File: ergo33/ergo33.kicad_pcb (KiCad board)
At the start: 2 copper layers, 171.4 x 117.8 mm, 113 parts, among them SW1 SW_Push, SW46 Rotary_Encoder_Switch, U1 ATmega32U4-AU, Y1 16MHz

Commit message: Start trace layout
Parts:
- removed F2: 500mA, Fuse:Fuse_1206_3216Metric
- added JP4: SolderJumper_2_Open, Jumper:SolderJumper-2_P1.3mm_Open_Pad1.0x1.5mm, B.Cu at (176.3, 40.5)
- SW46: footprint tunks-parts:RotaryEncoder_Alps_EC11E-Switch_Vertical_H20mm_30mm_knob -> Rotary_Encoder:RotaryEncoder_Alps_EC11E-Switch_Vertical_H20mm
- moved JP1 70.8 mm to (227.0, 24.2)
- moved R4 55.1 mm to (169.7, 76.0), turned to 0 degrees
- moved LED10 54.1 mm to (210.6, 106.7)
- moved C18 52.7 mm to (204.8, 106.5)
- moved C1 47.5 mm to (186.5, 70.5)
- moved LED7 46.9 mm to (78.9, 128.7)
- moved C15 46.9 mm to (74.1, 129.4)
- moved C5 45.6 mm to (179.7, 76.0)
- moved C2 42.0 mm to (186.5, 61.4)
- moved Y1 39.5 mm to (186.8, 65.8), turned to 135 degrees
- moved C17 38.8 mm to (152.6, 146.6)
- moved LED9 38.8 mm to (157.3, 145.8)
- moved SW1 38.2 mm to (186.4, 47.5), turned to 90 degrees
- moved U1 38.0 mm to (174.9, 66.2), turned to 270 degrees
- moved JLED1 37.7 mm to (210.3, 89.8)
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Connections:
- net Net-(F1-Pad1) renamed PWR_IN
- JP1 pad 1: LEDS -> (no net)
- SW46 pad A: ENC1 -> (no net)
- SW46 pad B: ENC2 -> (no net)
- U1 pad 1: Net-(U1-Pad1) -> (no net)
- U1 pad 10: Net-(U1-Pad10) -> (no net)
- U1 pad 11: Net-(U1-Pad11) -> (no net)
- U1 pad 12: Net-(U1-Pad12) -> (no net)
- U1 pad 18: Net-(U1-Pad18) -> (no net)
- U1 pad 19: Net-(U1-Pad19) -> (no net)
- U1 pad 20: Net-(U1-Pad20) -> (no net)
- U1 pad 21: Net-(U1-Pad21) -> (no net)
- U1 pad 22: Net-(U1-Pad22) -> (no net)
- U1 pad 25: Net-(U1-Pad25) -> (no net)
- U1 pad 26: Net-(U1-Pad26) -> (no net)
- U1 pad 27: Net-(U1-Pad27) -> (no net)
- U1 pad 28: Net-(U1-Pad28) -> (no net)
- U1 pad 29: Net-(U1-Pad29) -> (no net)
- U1 pad 30: Net-(U1-Pad30) -> (no net)
- U1 pad 31: Net-(U1-Pad31) -> (no net)
- U1 pad 32: Net-(U1-Pad32) -> (no net)
- U1 pad 36: Net-(U1-Pad36) -> (no net)
- U1 pad 37: Net-(U1-Pad37) -> (no net)
- U1 pad 38: Net-(U1-Pad38) -> (no net)
- U1 pad 39: Net-(U1-Pad39) -> (no net)
- U1 pad 40: Net-(U1-Pad40) -> (no net)
- U1 pad 41: Net-(U1-Pad41) -> (no net)
- U1 pad 42: Net-(U1-Pad42) -> (no net)
- U1 pad 8: Net-(U1-Pad8) -> (no net)
- U1 pad 9: Net-(U1-Pad9) -> (no net)
- USB1 pad 10: Net-(USB1-Pad10) -> (no net)
- USB1 pad 11: Net-(USB1-Pad11) -> (no net)
- USB1 pad 14: Net-(USB1-Pad14) -> (no net)
- USB1 pad 15: Net-(USB1-Pad15) -> (no net)
- USB1 pad 2: Net-(USB1-Pad2) -> (no net)
- USB1 pad 20: Net-(USB1-Pad20) -> (no net)
- USB1 pad 22: Net-(USB1-Pad22) -> (no net)
- USB1 pad 23: Net-(USB1-Pad23) -> (no net)
- USB1 pad 3: Net-(USB1-Pad3) -> (no net)
- USB1 pad 8: Net-(USB1-Pad8) -> (no net)
- USB2 pad 2: Net-(USB2-Pad2) -> (no net)
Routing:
- net +5V: track 0.00 -> 91.6 mm, vias 0 -> 2
- net GND: track 0.00 -> 62.3 mm, vias 0 -> 11
- net D+: track 0.00 -> 44.6 mm, vias 0 -> 5
- net D-: track 0.00 -> 43.1 mm, vias 0 -> 4
- net Net-(R1-Pad1): track 0.00 -> 23.7 mm, vias 0 -> 2
- net PWR_IN: track 0.00 -> 21.4 mm, vias 0 -> 2
- net Net-(R6-Pad2): track 0.00 -> 13.7 mm, vias 0 -> 1
- net Net-(JP2-Pad1): track 0.00 -> 11.8 mm
- net Net-(R2-Pad1): track 0.00 -> 11.0 mm
- net Net-(JP3-Pad1): track 0.00 -> 10.9 mm
- net Net-(C1-Pad2): track 0.00 -> 10.7 mm
- net Net-(C2-Pad2): track 0.00 -> 10.4 mm
- net Net-(R3-Pad1): track 0.00 -> 10.1 mm
- net Net-(R5-Pad2): track 0.00 -> 6.32 mm
- net Net-(JP4-Pad1): track 0.00 -> 4.85 mm
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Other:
- board size 171.4 x 117.8 mm -> 168.8 x 117 mm
- net class C data added: clearance 0.2, trace_width 0.2, via_dia 0.8, via_drill 0.4
- net class Power added: clearance 0.2, trace_width 0.375, via_dia 0.8, via_drill 0.4
- net class Power in added: clearance 0.2, trace_width 0.25, via_dia 0.8, via_drill 0.4

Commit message: Rerouting ergo33
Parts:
- moved LED10 52.6 mm to (163.4, 83.6)
- moved C18 51.7 mm to (158.1, 84.3)
- moved C12 40.0 mm to (47.0, 37.6)
- moved C17 40.0 mm to (154.5, 106.6)
- moved LED9 39.9 mm to (159.7, 105.9)
- moved JLED1 38.5 mm to (172.4, 82.9)
- moved LED6 36.3 mm to (42.9, 93.3)
- moved C14 36.0 mm to (37.6, 94.0)
- moved C13 34.3 mm to (47.0, 75.8)
- moved LED4 32.7 mm to (42.9, 35.8), turned to 90 degrees
- moved C9 30.6 mm to (149.4, 46.2), turned to 270 degrees
- moved C16 30.1 mm to (116.4, 104.5)
- moved LED8 30.0 mm to (121.6, 103.8)
- moved LED3 28.0 mm to (81.0, 43.4)
- moved C11 27.9 mm to (75.7, 44.1)
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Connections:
- U1 pad 37: (no net) -> ROW4
- U1 pad 38: (no net) -> ROW3
- U1 pad 39: (no net) -> ROW2
- U1 pad 40: (no net) -> ROW1
- U1 pad 41: (no net) -> ROW0
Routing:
- net ROW0: track 0.00 -> 158.7 mm
- net +5V: track 91.6 -> 244.9 mm, vias 2 -> 6
- net ROW2: track 0.00 -> 145.2 mm
- net ROW1: track 0.00 -> 143.7 mm
- net ROW3: track 0.00 -> 126.5 mm
- net COL1: track 0.00 -> 85.7 mm, vias 0 -> 5
- net COL0: track 0.00 -> 84.7 mm, vias 0 -> 5
- net COL4: track 0.00 -> 62.8 mm, vias 0 -> 4
- net COL2: track 0.00 -> 62.8 mm, vias 0 -> 4
- net COL6: track 0.00 -> 62.8 mm, vias 0 -> 4
- net COL3: track 0.00 -> 62.7 mm, vias 0 -> 4
- net COL5: track 0.00 -> 62.7 mm, vias 0 -> 4
- net GND: track 62.3 -> 104.8 mm, vias 11 -> 20
- net Net-(LED3-Pad2): track 0.00 -> 37.5 mm
- net Net-(LED2-Pad2): track 0.00 -> 34.5 mm
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- added copper zone on F.Cu, net GND
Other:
- board size 168.8 x 117 mm -> 168.9 x 117 mm

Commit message: Finish ergo33 routing v1
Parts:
- moved JP1 83.0 mm to (168.8, 83.4)
- moved C15 10.6 mm to (86.2, 101.4), turned to 90 degrees
- moved C14 10.5 mm to (48.0, 92.6), turned to 90 degrees
- moved C16 7.95 mm to (124.3, 103.6), turned to 90 degrees
- moved D43 6.70 mm to (127.0, 119.7)
- moved D44 5.95 mm to (147.5, 120.7)
- moved D45 5.78 mm to (165.9, 125.7)
- moved C17 5.39 mm to (156.5, 101.6), turned to 180 degrees
- moved LED10 4.11 mm to (159.8, 85.7), turned to 270 degrees
- moved C18 4.03 mm to (159.1, 80.4), turned to 180 degrees
- moved LED9 2.70 mm to (157.2, 106.8), turned to 270 degrees
- moved LED8 2.64 mm to (119.1, 104.3), turned to 180 degrees
- moved D46 1.73 mm to (169.0, 102.9), turned to 0 degrees
- moved R4 1.50 mm to (169.6, 75.0)
- moved JLED1 1.00 mm to (172.4, 83.9)
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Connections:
- JP1 pad 1: (no net) -> Net-(JP1-Pad1)
- JP1 pad 2: Net-(JP1-Pad2) -> LEDS
- LED1 pad 4: Net-(JP1-Pad2) -> Net-(JP1-Pad1)
- U1 pad 25: (no net) -> LEDS
- U1 pad 26: (no net) -> COL6
- U1 pad 27: (no net) -> COL5
- U1 pad 28: (no net) -> COL4
- U1 pad 29: (no net) -> COL3
- U1 pad 30: (no net) -> COL2
- U1 pad 31: (no net) -> COL1
- U1 pad 32: (no net) -> COL0
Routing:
- net +5V: track 244.9 -> 523.0 mm, vias 6 -> 10
- net ROW4: track 20.1 -> 202.1 mm, vias 0 -> 2
- net COL0: track 84.7 -> 251.1 mm, vias 5 -> 6
- net COL3: track 62.7 -> 223.3 mm, vias 4 -> 6
- net COL1: track 85.7 -> 234.2 mm, vias 5 -> 6
- net COL4: track 62.8 -> 205.4 mm, vias 4 -> 6
- net COL2: track 62.8 -> 190.6 mm, vias 4 -> 5
- net COL5: track 62.7 -> 186.7 mm, vias 4 -> 6
- net COL6: track 62.8 -> 156.1 mm, vias 4 -> 6
- net GND: track 104.8 -> 163.5 mm, vias 20 -> 28
- net Net-(JP1-Pad1): track 0.00 -> 42.4 mm, vias 0 -> 2
- net ROW3: track 126.5 -> 166.9 mm, vias 0 -> 2
- net Net-(LED6-Pad2): track 0.00 -> 35.5 mm
- net Net-(LED8-Pad2): track 0.00 -> 35.5 mm
- net Net-(LED4-Pad2): track 0.00 -> 34.8 mm, vias 0 -> 2
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
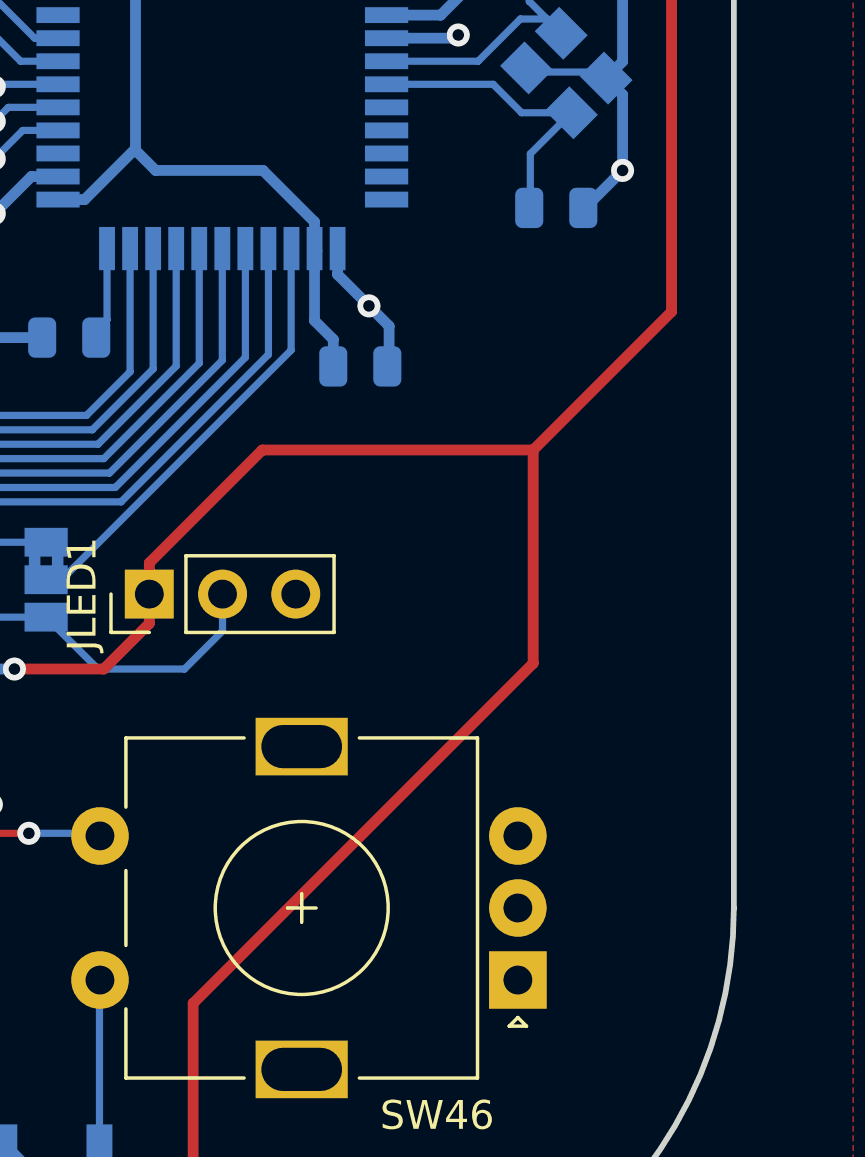
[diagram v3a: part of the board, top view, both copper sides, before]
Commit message: Fix ergo33 routing
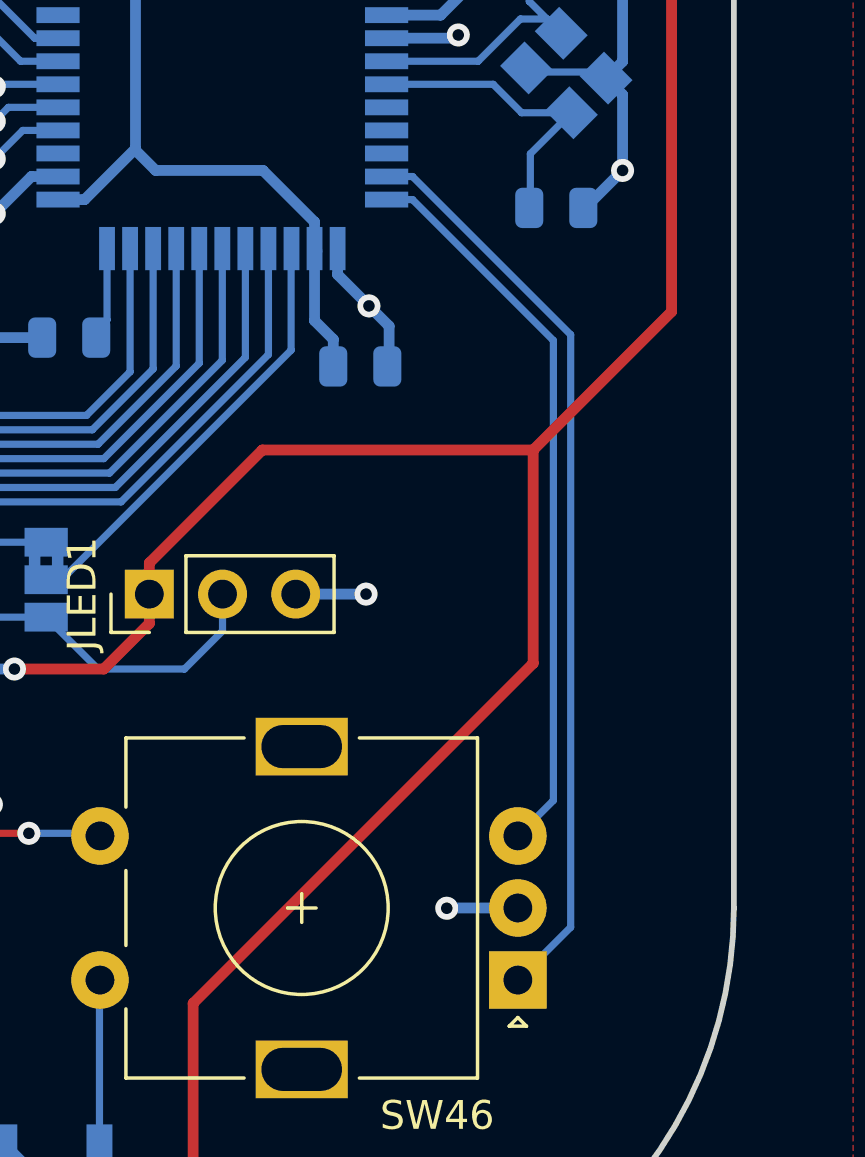
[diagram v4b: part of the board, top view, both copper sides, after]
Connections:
- SW46 pad A: (no net) -> ENC1
- SW46 pad B: (no net) -> ENC2
- U1 pad 21: (no net) -> ENC1
- U1 pad 22: (no net) -> ENC2
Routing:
- net ENC1: track 0.00 -> 31.8 mm
- net ENC2: track 0.00 -> 25.5 mm
- net GND: track 163.5 -> 168.4 mm, vias 28 -> 30

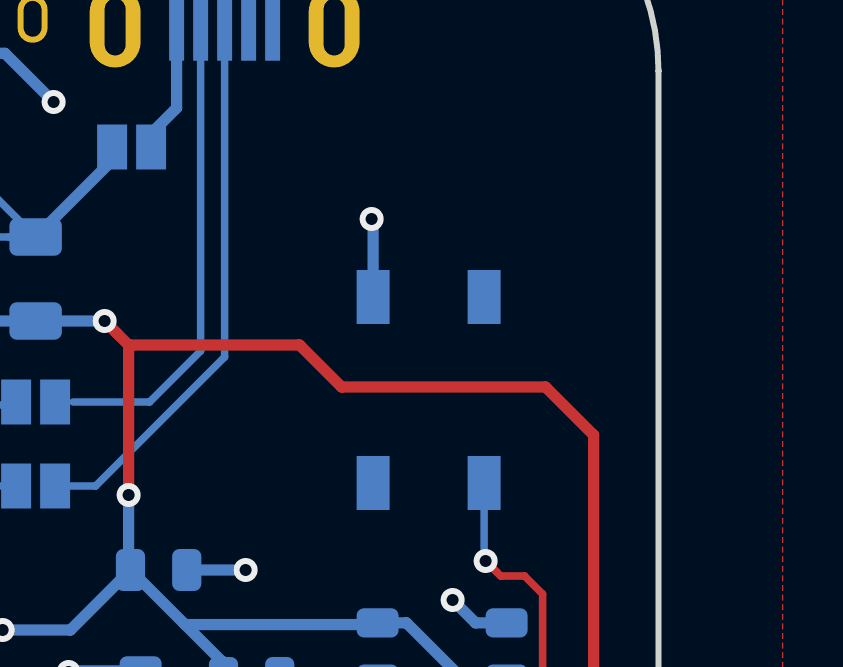
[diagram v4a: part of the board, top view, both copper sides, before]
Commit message: Add arc suppression cap to ergo33
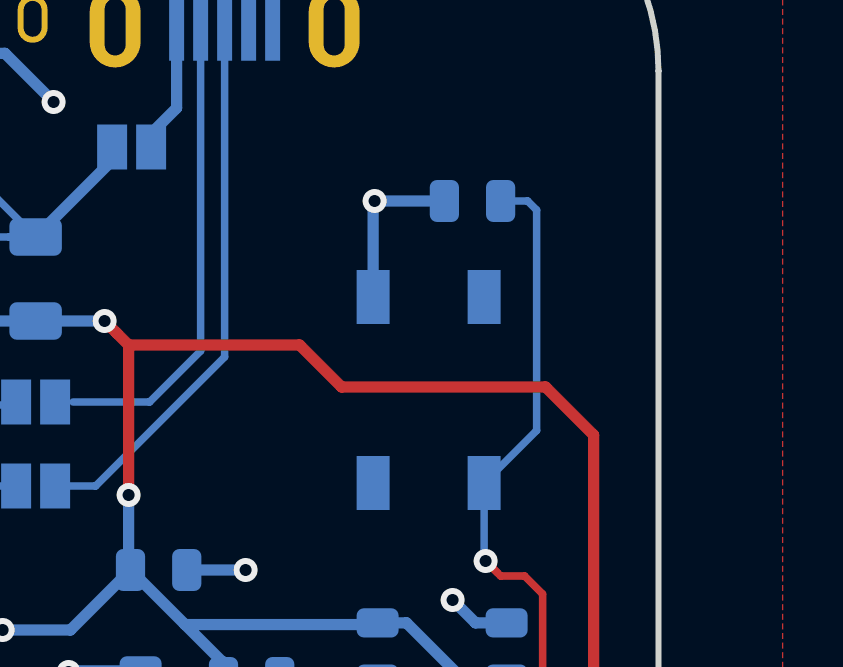
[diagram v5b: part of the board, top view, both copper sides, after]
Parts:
- added C19: 510pF, Capacitor_SMD:C_0805_2012Metric, B.Cu at (186.5, 40.2)
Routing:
- net Net-(C19-Pad1): track 24.8 -> 35.9 mm
- net GND: track 168.4 -> 171.3 mm

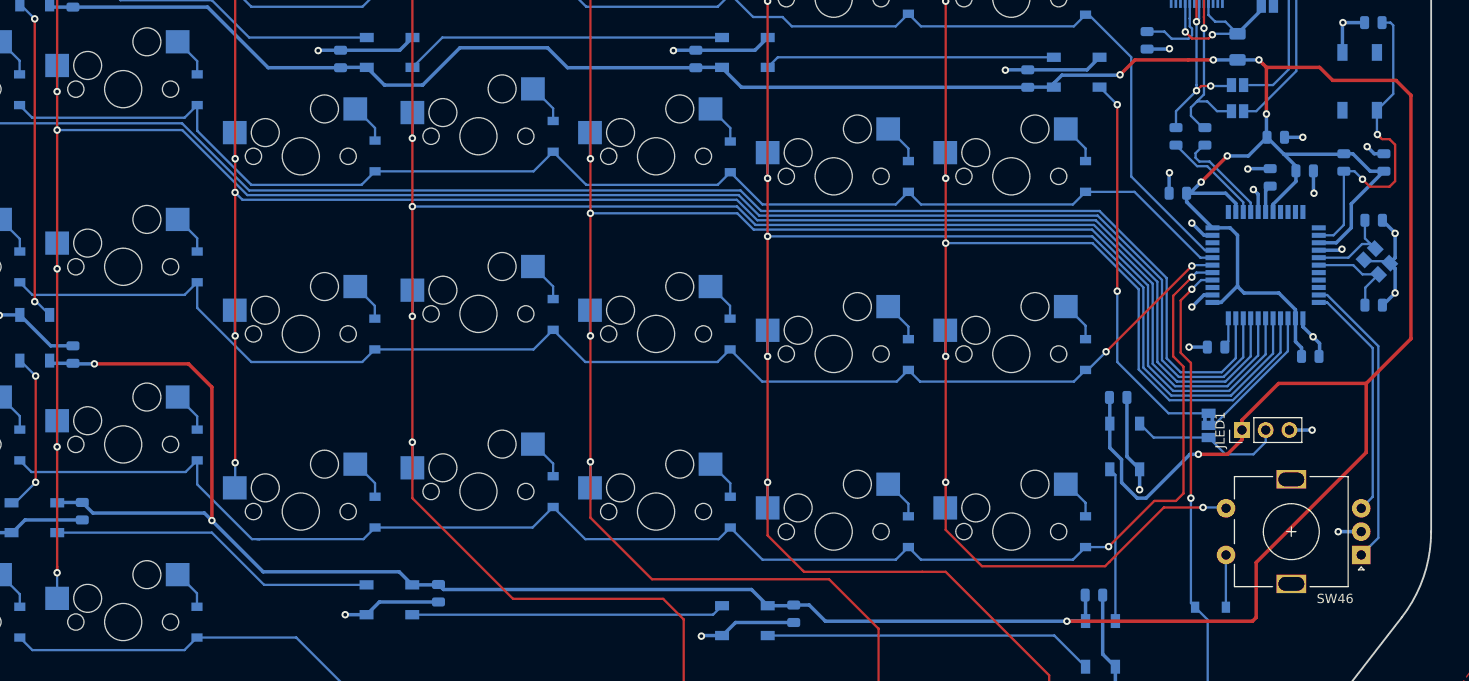
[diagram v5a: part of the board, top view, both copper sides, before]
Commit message: Reroute ergo33 MCU area
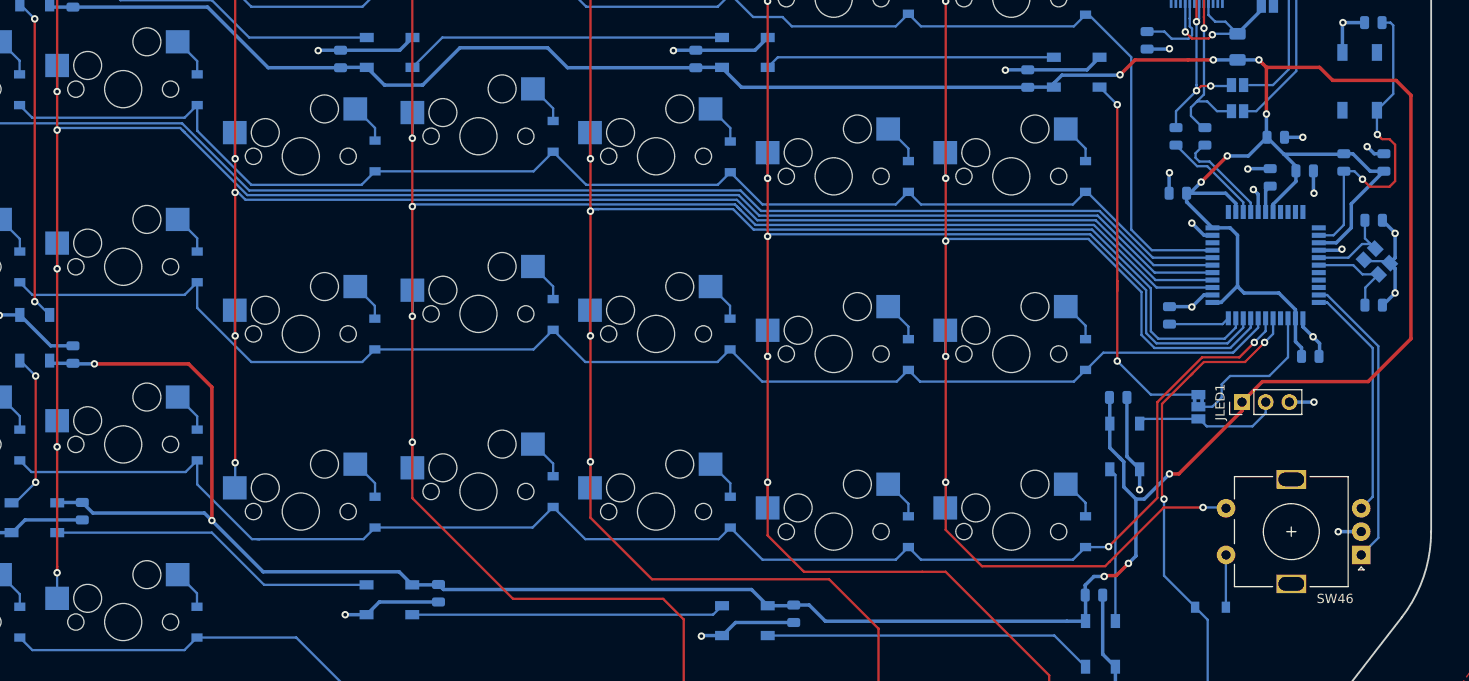
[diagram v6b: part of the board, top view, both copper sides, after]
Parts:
- moved R4 6.05 mm to (164.6, 71.6), turned to 270 degrees
- moved JLED1 3.00 mm to (172.4, 80.9)
- moved JP1 2.28 mm to (167.7, 81.4)
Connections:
- U1 pad 26: COL6 -> (no net)
- U1 pad 27: COL5 -> ROW4
- U1 pad 28: COL4 -> ROW3
- U1 pad 29: COL3 -> ROW2
- U1 pad 30: COL2 -> COL6
- U1 pad 31: COL1 -> COL5
- U1 pad 32: COL0 -> COL4
- U1 pad 36: (no net) -> COL3
- U1 pad 37: ROW4 -> COL2
- U1 pad 38: ROW3 -> COL1
- U1 pad 39: ROW2 -> COL0
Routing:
- net +5V: track 523.0 -> 487.0 mm, vias 10 -> 11
- net COL3: track 223.3 -> 204.3 mm
- net COL2: track 190.6 -> 171.7 mm
- net COL1: track 234.2 -> 216.7 mm
- net COL0: track 251.1 -> 233.9 mm
- net COL5: track 186.7 -> 175.1 mm
- net COL6: track 156.1 -> 145.0 mm
- net COL4: track 205.4 -> 194.6 mm
- net ROW0: track 158.7 -> 162.8 mm
- net ROW3: track 166.9 -> 163.4 mm
- net Net-(R4-Pad2): track 3.24 -> 6.57 mm
- net ROW2: track 145.3 -> 148.6 mm, vias 2 -> 0
- net ROW4: track 202.1 -> 204.4 mm
- net LEDS: track 15.3 -> 16.8 mm
- net LEDS2: track 16.7 -> 15.8 mm
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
